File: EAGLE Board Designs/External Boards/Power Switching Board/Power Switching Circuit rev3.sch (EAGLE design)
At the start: 62 parts, among them J1 CONNECTOR-3_, J2 CONNECTOR-4_SOURIAU_, J3 CONNECTOR-4_SOURIAU_, K1 J115F11A6, Q1 TRANSISTOR_N_MOS_2-7K1S_TK100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, Q2 TRANSISTOR_N_MOS_2-7K1S_TK100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, Q3 TRANSISTOR_N_MOS_2-7K1S_TK100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, Q4 TRANSISTOR_N_MOS_2-7K1S_TK100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, U1 LTC4421

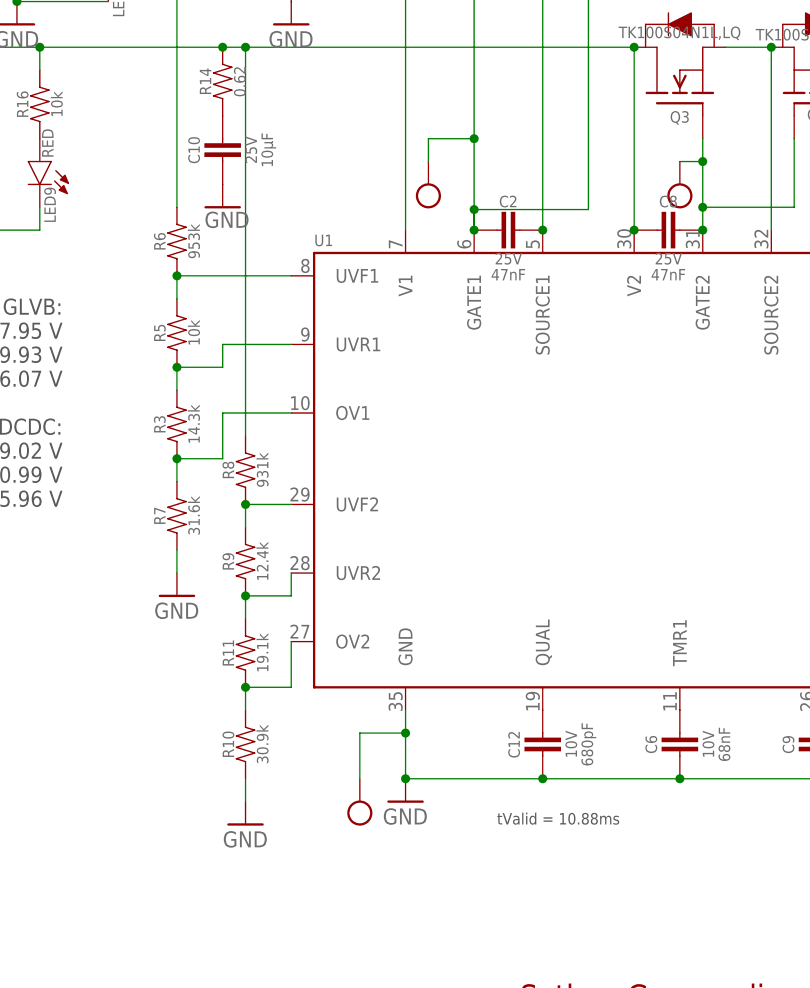
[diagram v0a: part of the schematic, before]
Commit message: Replaced test points with ones in library
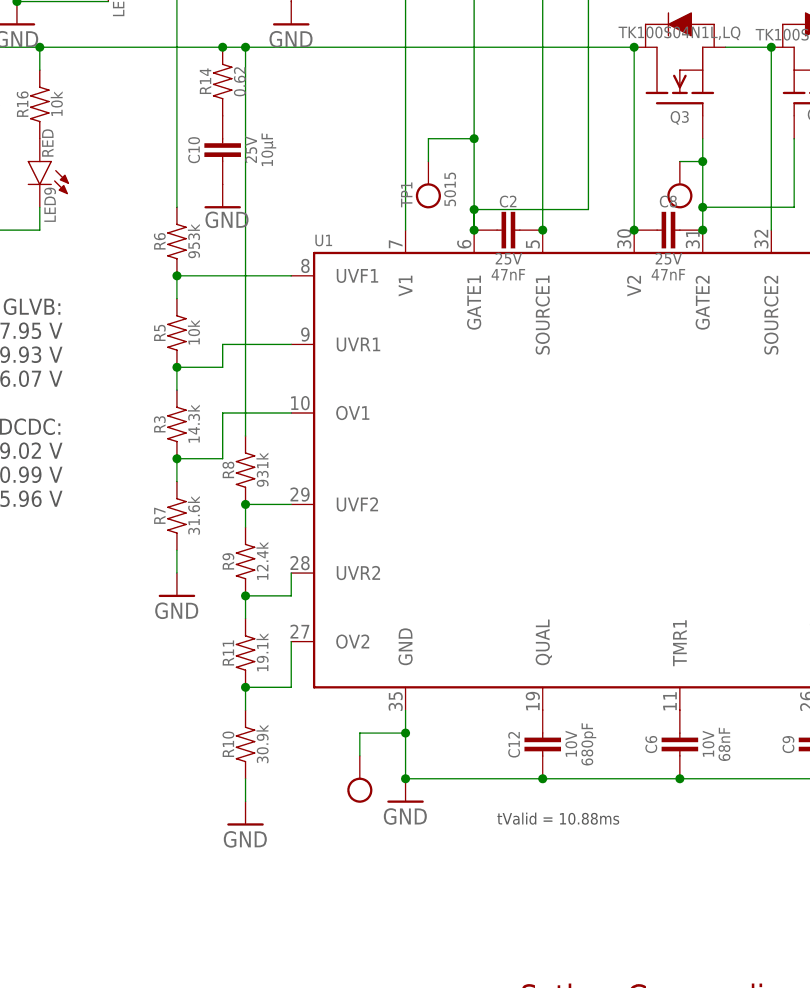
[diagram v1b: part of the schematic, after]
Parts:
- removed U$10: TEST_POINTMICRO_MINIATURE, HyTechDevices:TEST_POINTMICRO_MINIATURE
- added TP1: TEST_POINT, HyTechDevices:TEST_POINT
- U$11, U$7, U$8, U$9: value TEST_POINTMICRO_MINIATURE -> TEST_POINT; device HyTechDevices:TEST_POINTMICRO_MINIATURE -> HyTechDevices:TEST_POINT
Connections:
- net GATE1: now also TP1.P$1; no longer U$10.P$1
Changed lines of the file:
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@@
 <part name="R1" library="HyTechDevices" deviceset="RESISTOR_SENSE" device=""/>
 <part name="C1" library="HyTechDevices" deviceset="CAPACITOR_POLARIZED" device=""/>
-<part name="U$7" library="HyTechDevices" deviceset="TEST_POINT" device="MICRO_MINIATURE"/>
-<part name="U$8" library="HyTechDevices" deviceset="TEST_POINT" device="MICRO_MINIATURE"/>
-<part name="U$9" library="HyTechDevices" deviceset="TEST_POINT" device="MICRO_MINIATURE"/>
-<part name="U$10" library="HyTechDevices" deviceset="TEST_POINT" device="MICRO_MINIATURE"/>
+<part name="U$7" library="HyTechDevices" deviceset="TEST_POINT" device=""/>
+<part name="U$8" library="HyTechDevices" deviceset="TEST_POINT" device=""/>
+<part name="U$9" library="HyTechDevices" deviceset="TEST_POINT" device=""/>
 <part name="LED9" library="HyTechDevices" deviceset="LED_?_*" device="0603" technology="RED" value="RED"/>
 <part name="R16" library="HyTechDevices" deviceset="RESISTOR" device="0603" value="10k"/>
@@
 <part name="Q3" library="HyTechDevices" deviceset="TRANSISTOR_N_MOS_?_*" device="2-7K1S" technology="TK100S04N1L,LQ"/>
 <part name="RN2" library="HyTechDevices" deviceset="RESISTOR_NETWORK_4_*" device="" technology="10K"/>
-<part name="U$11" library="HyTechDevices" deviceset="TEST_POINT" device="MICRO_MINIATURE"/>
+<part name="U$11" library="HyTechDevices" deviceset="TEST_POINT" device=""/>
 <part name="F1" library="HyTechDevices" deviceset="FUSE_?_*" device="0885" technology="1.6"/>
 <part name="F2" library="HyTechDevices" deviceset="FUSE_?_*" device="0885" technology="1.6"/>
@@
 <part name="C6" library="HyTechDevices" deviceset="CAPACITOR_?_*" device="0603" technology="10V_68NF"/>
 <part name="C9" library="HyTechDevices" deviceset="CAPACITOR_?_*" device="0603" technology="10V_68NF"/>
+<part name="TP1" library="HyTechDevices" deviceset="TEST_POINT" device=""/>
 </parts>
 <sheets>
@@
 <attribute name="NAME" x="86.36" y="39.37" size="1.27" layer="95" rot="R270" align="bottom-center"/>
 </instance>
-<instance part="U$7" gate="G$1" x="10.16" y="10.16" smashed="yes" rot="R270"/>
-<instance part="U$8" gate="G$1" x="53.34" y="-55.88" smashed="yes" rot="R270"/>
-<instance part="U$9" gate="G$1" x="60.96" y="5.08" smashed="yes"/>
-<instance part="U$10" gate="G$1" x="-17.78" y="10.16" smashed="yes" rot="R270"/>
+<instance part="U$7" gate="G$1" x="10.16" y="10.16" smashed="yes" rot="R90"/>
+<instance part="U$8" gate="G$1" x="53.34" y="-55.88" smashed="yes" rot="R90"/>
+<instance part="U$9" gate="G$1" x="60.96" y="5.08" smashed="yes" rot="R180"/>
 <instance part="LED9" gate="LED" x="-60.96" y="10.16" smashed="yes" rot="R270">
 <attribute name="VALUE" x="-59.436" y="14.732" size="1.27" layer="95" rot="R270" align="top-center"/>
@@
 <attribute name="RESISTANCE" x="100.33" y="-11.43" size="1.27" layer="96" align="top-center"/>
 </instance>
-<instance part="U$11" gate="G$1" x="-25.4" y="-58.42" smashed="yes" rot="R270"/>
+<instance part="U$11" gate="G$1" x="-25.4" y="-55.88" smashed="yes" rot="R90"/>
 <instance part="F1" gate="G$1" x="-109.22" y="27.94" smashed="yes">
 <attribute name="NAME" x="-110.49" y="29.21" size="1.27" layer="95" align="bottom-center"/>
@@
 <attribute name="VOLTAGE" x="27.94" y="-52.07" size="1.27" layer="96" rot="R90" align="top-center"/>
 <attribute name="CAPACITANCE" x="29.718" y="-52.07" size="1.27" layer="96" rot="R90" align="top-center"/>
+</instance>
+<instance part="TP1" gate="G$1" x="-17.78" y="10.16" smashed="yes" rot="R90">
+<attribute name="NAME" x="-19.558" y="7.62" size="1.27" layer="95" rot="R90"/>
+<attribute name="MPN" x="-16.002" y="7.62" size="1.27" layer="95" rot="R90" align="top-left"/>
 </instance>
 </instances>
@@
 <pinref part="U1" gate="G$1" pin="GND"/>
 <pinref part="U$11" gate="G$1" pin="P$1"/>
-<wire x1="-25.4" y1="-55.88" x2="-25.4" y2="-50.8" width="0.1524" layer="91"/>
+<wire x1="-25.4" y1="-53.34" x2="-25.4" y2="-50.8" width="0.1524" layer="91"/>
 <wire x1="-25.4" y1="-50.8" x2="-20.32" y2="-50.8" width="0.1524" layer="91"/>
 <wire x1="-20.32" y1="-50.8" x2="-20.32" y2="-48.26" width="0.1524" layer="91"/>
@@
 <pinref part="Q1" gate="G$1" pin="G"/>
 <pinref part="Q2" gate="G$1" pin="G"/>
-<pinref part="U$10" gate="G$1" pin="P$1"/>
 <wire x1="-17.78" y1="12.7" x2="-17.78" y2="15.24" width="0.1524" layer="91"/>
 <wire x1="-17.78" y1="15.24" x2="-12.7" y2="15.24" width="0.1524" layer="91"/>
 <junction x="-12.7" y="15.24"/>
 <pinref part="C2" gate="G$1" pin="2"/>
-</segment>
-</net>
+<pinref part="TP1" gate="G$1" pin="P$1"/>
+</segment>
+</net>

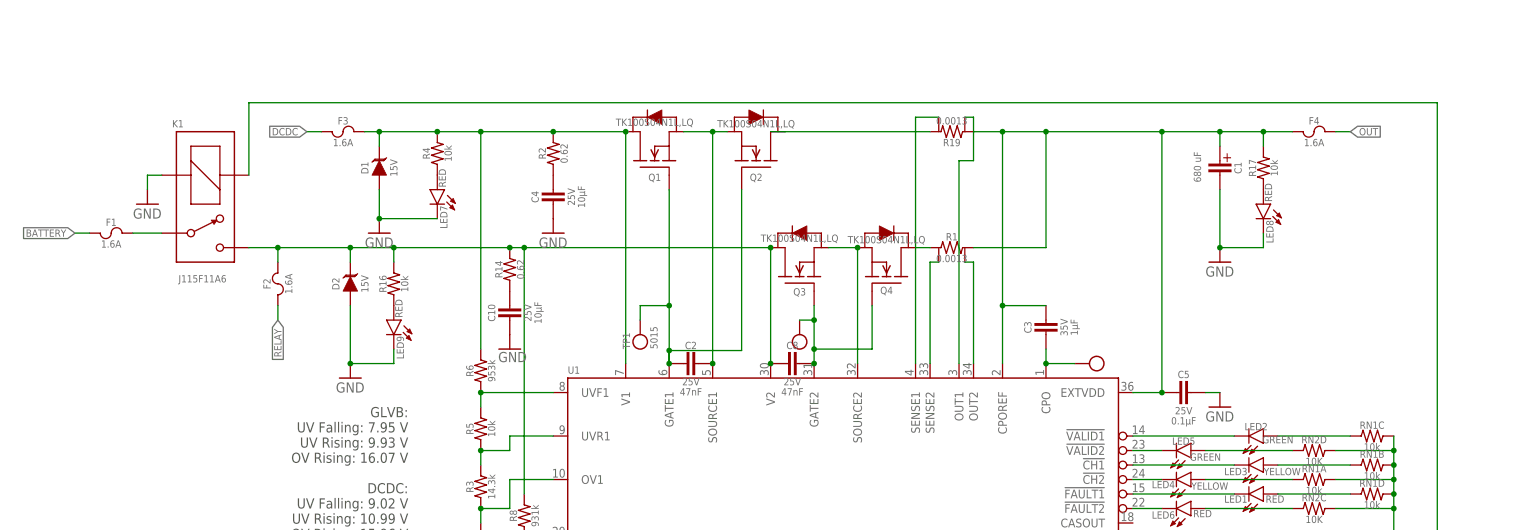
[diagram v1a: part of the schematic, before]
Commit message: Added SS Relay to schematic
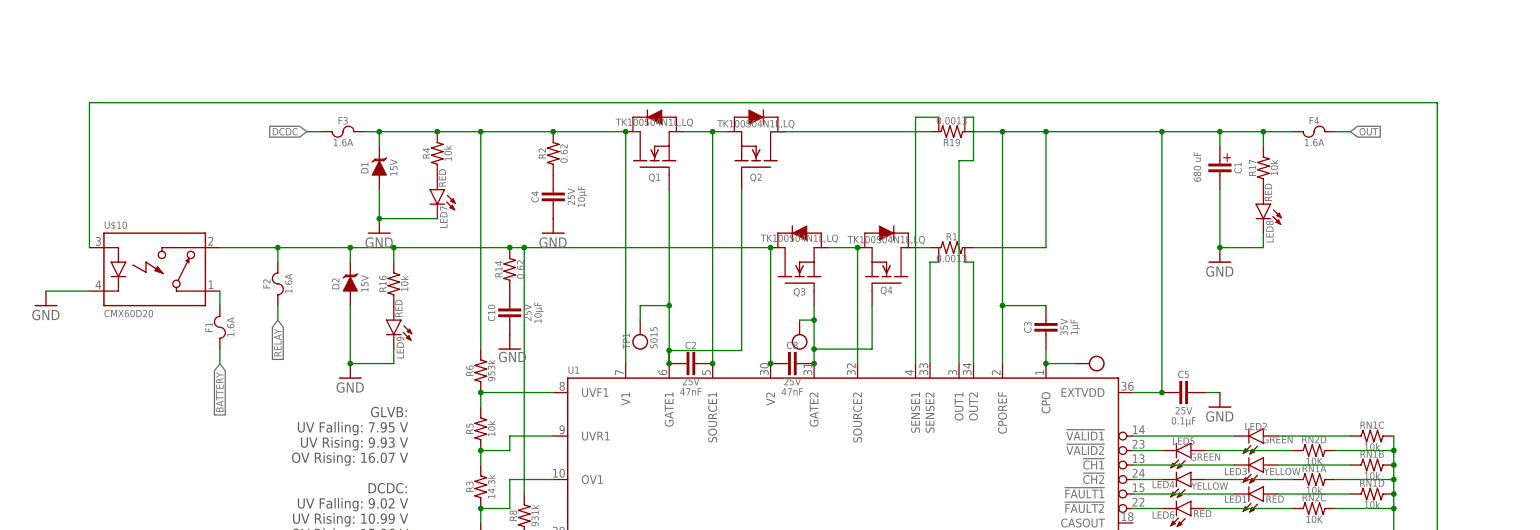
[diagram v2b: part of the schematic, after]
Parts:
- removed K1: J115F11A6, HyTechDevices:J115F11A6
- added U$10: RELAY_SOLIDSTATE_NO_CMX60D20, HyTechDevices:RELAY_SOLIDSTATE_NO_CMX60D20
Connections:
- net GND: now also U$10.CONTROL-; no longer K1.COIL-
- net N$12: now also U$10.CONTACT1; no longer K1.P
- net N$16: now also U$10.CONTROL+; no longer K1.COIL+
- net RELAY: now also U$10.CONTACT2; no longer K1.S
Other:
- moved on the sheet: F1
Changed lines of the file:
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@@
 <part name="LED2" library="HyTechDevices" deviceset="LED_?_*" device="0603" technology="GREEN" value="GREEN"/>
 <part name="GND3" library="HyTechSymbols" deviceset="GND" device=""/>
-<part name="K1" library="HyTechDevices" deviceset="J115F11A*6*" device=""/>
 <part name="GND4" library="HyTechSupplies" deviceset="GND" device=""/>
 <part name="R10" library="HyTechDevices" deviceset="RESISTOR_?_*" device="0603" technology="30.9K" value="30.9k"/>
@@
 <part name="C9" library="HyTechDevices" deviceset="CAPACITOR_?_*" device="0603" technology="10V_68NF"/>
 <part name="TP1" library="HyTechDevices" deviceset="TEST_POINT" device=""/>
+<part name="U$10" library="HyTechDevices" deviceset="RELAY_SOLIDSTATE_NO_?*" device="" technology="CMX60D20"/>
 </parts>
 <sheets>
@@
 <attribute name="VALUE" x="81.28" y="-5.08" size="1.778" layer="96"/>
 </instance>
-<instance part="K1" gate="G$1" x="-99.06" y="45.72" smashed="yes">
-<attribute name="NAME" x="-98.806" y="46.482" size="1.27" layer="95" align="bottom-center"/>
-<attribute name="VALUE" x="-94.488" y="20.574" size="1.27" layer="96" align="top-center"/>
-</instance>
-<instance part="GND4" gate="1" x="-104.14" y="33.02" smashed="yes">
-<attribute name="VALUE" x="-106.68" y="30.48" size="1.778" layer="96"/>
+<instance part="GND4" gate="1" x="-121.92" y="15.24" smashed="yes">
+<attribute name="VALUE" x="-124.46" y="12.7" size="1.778" layer="96"/>
 </instance>
 <instance part="R10" gate="G$1" x="-38.1" y="-50.8" smashed="yes" rot="R90">
@@
 </instance>
 <instance part="U$11" gate="G$1" x="-25.4" y="-55.88" smashed="yes" rot="R90"/>
-<instance part="F1" gate="G$1" x="-109.22" y="27.94" smashed="yes">
-<attribute name="NAME" x="-110.49" y="29.21" size="1.27" layer="95" align="bottom-center"/>
-<attribute name="CURRENT" x="-110.49" y="26.67" size="1.27" layer="96" align="top-center"/>
+<instance part="F1" gate="G$1" x="-91.44" y="12.7" smashed="yes" rot="R90">
+<attribute name="NAME" x="-92.71" y="11.43" size="1.27" layer="95" rot="R90" align="bottom-center"/>
+<attribute name="CURRENT" x="-90.17" y="11.43" size="1.27" layer="96" rot="R90" align="top-center"/>
 </instance>
 <instance part="F2" gate="G$1" x="-81.28" y="20.32" smashed="yes" rot="R90">
@@
 <attribute name="NAME" x="-19.558" y="7.62" size="1.27" layer="95" rot="R90"/>
 <attribute name="MPN" x="-16.002" y="7.62" size="1.27" layer="95" rot="R90" align="top-left"/>
+</instance>
+<instance part="U$10" gate="G$1" x="-111.76" y="27.94" smashed="yes">
+<attribute name="NAME" x="-111.76" y="28.702" size="1.27" layer="95"/>
+<attribute name="MPN" x="-111.76" y="14.478" size="1.27" layer="96" align="top-left"/>
 </instance>
 </instances>
@@
 <pinref part="GND14" gate="1" pin="GND"/>
 <wire x1="48.26" y1="-66.04" x2="48.26" y2="-68.58" width="0.1524" layer="91"/>
-</segment>
-<segment>
-<pinref part="GND4" gate="1" pin="GND"/>
-<pinref part="K1" gate="G$1" pin="COIL-"/>
-<wire x1="-104.14" y1="35.56" x2="-104.14" y2="38.1" width="0.1524" layer="91"/>
-<wire x1="-104.14" y1="38.1" x2="-101.6" y2="38.1" width="0.1524" layer="91"/>
 </segment>
 <segment>
@@
 <pinref part="C10" gate="G$1" pin="2"/>
 </segment>
+<segment>
+<pinref part="U$10" gate="G$1" pin="CONTROL-"/>
+<pinref part="GND4" gate="1" pin="GND"/>
+<wire x1="-114.3" y1="17.78" x2="-121.92" y2="17.78" width="0.1524" layer="91"/>
+</segment>
 </net>
 <net name="BATTERY" class="0">
@@
 <segment>
 <pinref part="F1" gate="G$1" pin="1"/>
-<wire x1="-114.3" y1="27.94" x2="-116.84" y2="27.94" width="0.1524" layer="91"/>
-<label x="-116.84" y="27.94" size="1.27" layer="95" rot="R180" xref="yes"/>
+<wire x1="-91.44" y1="7.62" x2="-91.44" y2="5.08" width="0.1524" layer="91"/>
+<label x="-91.44" y="5.08" size="1.27" layer="95" rot="R270" xref="yes"/>
 </segment>
 </net>
@@
 <segment>
 <pinref part="R14" gate="G$1" pin="2"/>
-<pinref part="K1" gate="G$1" pin="S"/>
-<wire x1="-86.36" y1="25.4" x2="-81.28" y2="25.4" width="0.1524" layer="91"/>
 <pinref part="R16" gate="G$1" pin="2"/>
 <wire x1="-81.28" y1="25.4" x2="-68.58" y2="25.4" width="0.1524" layer="91"/>
@@
 <pinref part="C8" gate="G$1" pin="2"/>
 <junction x="5.08" y="5.08"/>
+<pinref part="U$10" gate="G$1" pin="CONTACT2"/>
+<wire x1="-81.28" y1="25.4" x2="-91.44" y2="25.4" width="0.1524" layer="91"/>
 </segment>
 <segment>
@@
 </segment>
 </net>
-<net name="N$12" class="0">
-<segment>
-<pinref part="K1" gate="G$1" pin="P"/>
-<pinref part="F1" gate="G$1" pin="2"/>
-<wire x1="-101.6" y1="27.94" x2="-106.68" y2="27.94" width="0.1524" layer="91"/>
-</segment>
-</net>
 <net name="N$16" class="0">
 <segment>
@@
 <wire x1="71.12" y1="-35.56" x2="76.2" y2="-35.56" width="0.1524" layer="91"/>
 <wire x1="76.2" y1="-35.56" x2="81.28" y2="-35.56" width="0.1524" layer="91"/>
-<pinref part="K1" gate="G$1" pin="COIL+"/>
 <wire x1="81.28" y1="-35.56" x2="121.92" y2="-35.56" width="0.1524" layer="91"/>
-<wire x1="-86.36" y1="38.1" x2="-86.36" y2="50.8" width="0.1524" layer="91"/>
-<wire x1="-86.36" y1="50.8" x2="121.92" y2="50.8" width="0.1524" layer="91"/>
+<wire x1="-114.3" y1="50.8" x2="121.92" y2="50.8" width="0.1524" layer="91"/>
 <wire x1="121.92" y1="50.8" x2="121.92" y2="-35.56" width="0.1524" layer="91"/>
 <pinref part="U1" gate="G$1" pin="!DISABLE2"/>
@@
 <pinref part="D4" gate="G$1" pin="C"/>
 <wire x1="78.74" y1="-55.88" x2="81.28" y2="-55.88" width="0.1524" layer="91"/>
+<pinref part="U$10" gate="G$1" pin="CONTROL+"/>
+<wire x1="-114.3" y1="50.8" x2="-114.3" y2="25.4" width="0.1524" layer="91"/>
 </segment>
 </net>
@@
 </segment>
 </net>
+<net name="N$12" class="0">
+<segment>
+<pinref part="U$10" gate="G$1" pin="CONTACT1"/>
+<pinref part="F1" gate="G$1" pin="2"/>
+<wire x1="-91.44" y1="15.24" x2="-91.44" y2="17.78" width="0.1524" layer="91"/>
+</segment>
+</net>
